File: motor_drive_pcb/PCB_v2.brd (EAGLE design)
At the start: 27 parts, among them IC1 MCP604P, J1 FRDM-K64F

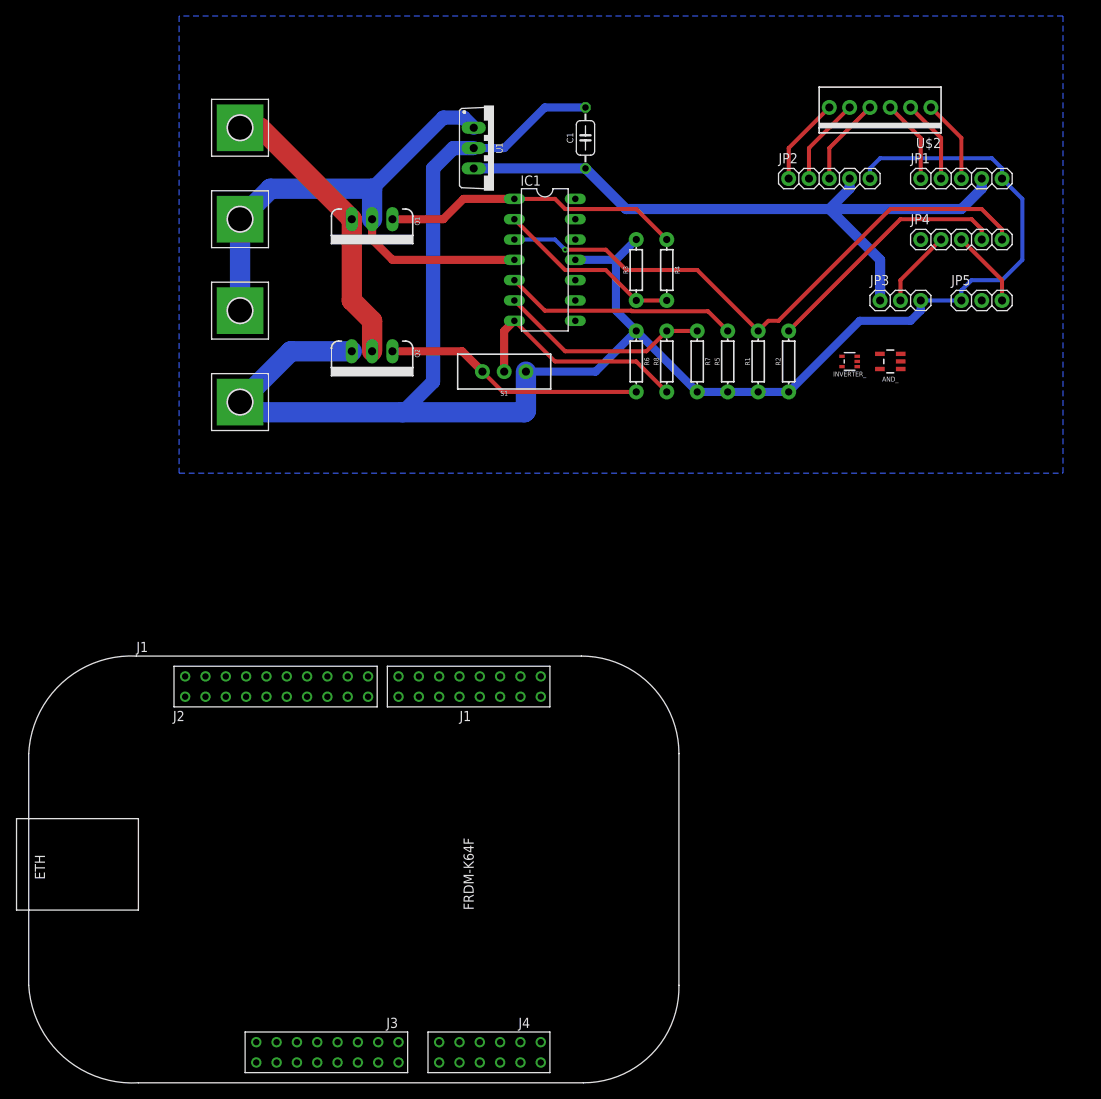
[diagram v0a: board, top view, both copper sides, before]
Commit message: updated pcb and encoder schematics and boards
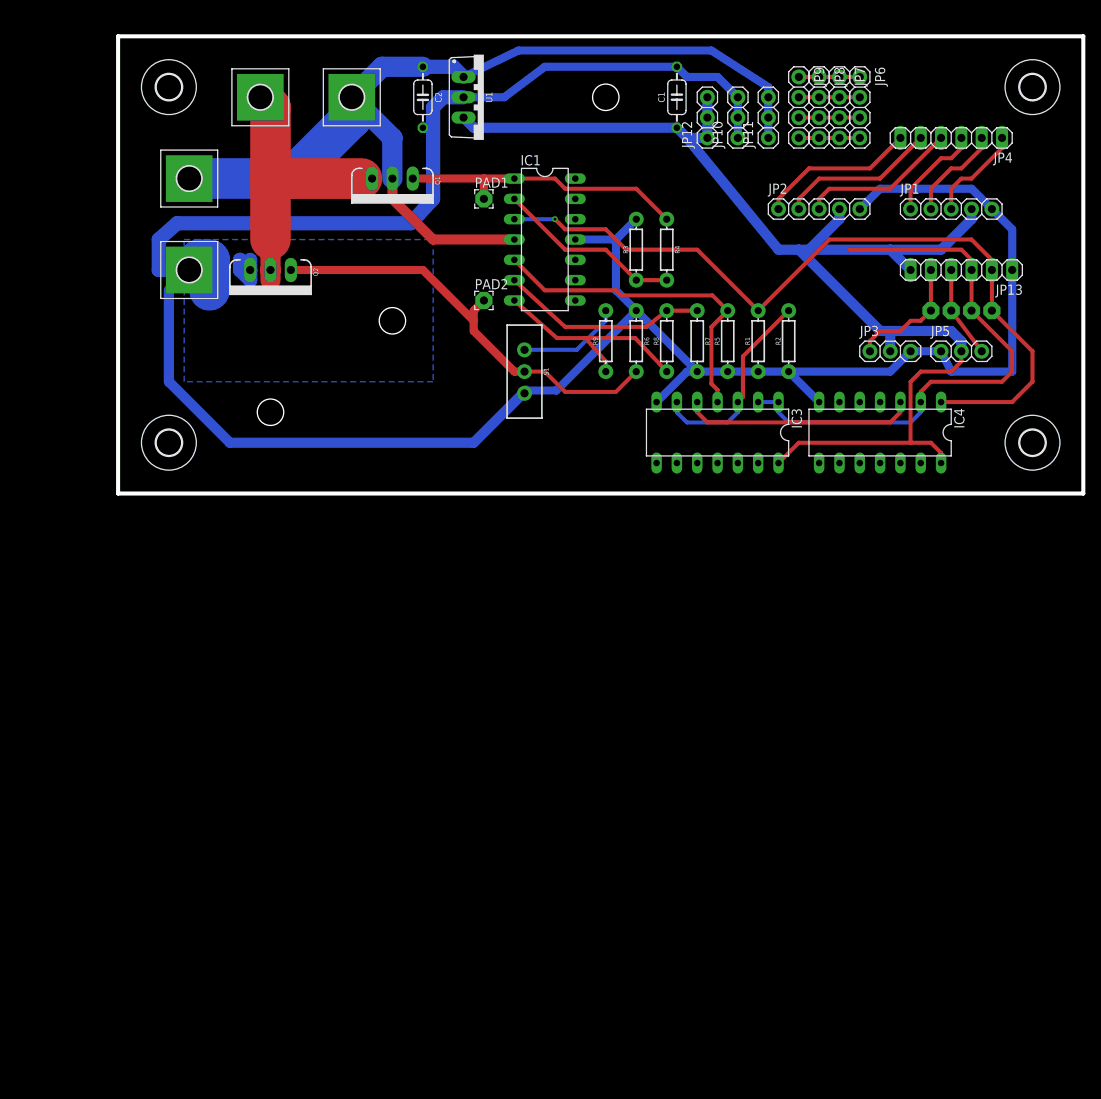
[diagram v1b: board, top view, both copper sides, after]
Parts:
- removed AND_: (no value), SparkFun-IC-Logic:SOT23-5
- removed INVERTER_: (no value), SparkFun-IC-Logic:SOT353
- removed J1: FRDM-K64F, ee192:FRDM-K64F
- removed U$2: M06, ee192:1X06-MTA
- added C2: (no value), bt_rcl:C075
- added H1, H2, H3, H4: MOUNT-HOLE3.2, holes:3,2
- added IC3: 4081N, 40xx:DIL14
- added IC4: 4030N, 40xx:DIL14
- added JP10, JP11, JP12: (no value), ee192:1X03
- added JP13: (no value), pinhead:1X06
- added JP6, JP7, JP8, JP9: (no value), ee192:1X04
- added PAD1, PAD2, PAD3, PAD5, PAD6, PAD7: (no value), wirepad:2,15/1,0
- added R9: 100, SparkFun-Resistors:AXIAL-0.3
- JP4: device ee192:1X05 -> pinhead:1X06
- moved BATT+1 20.7 mm to (-17.8, 45.7)
- moved BATT+ 17.7 mm to (-38.1, 35.6)
- moved BATT- 17.7 mm to (-38.1, 24.1)
- moved Q2 16.3 mm to (-27.9, 24.1)
- moved JP4 12.8 mm to (57.1, 40.6), turned to 180 degrees
- moved C1 12.5 mm to (22.9, 45.7)
- moved JP5 6.84 mm to (58.4, 14.0)
- moved U1 6.48 mm to (-3.81, 45.7)
- moved JP3 6.48 mm to (49.5, 14.0)
- moved Q1 5.68 mm to (-12.7, 35.6)
- moved BATT-1 4.58 mm to (-29.2, 45.7)
- moved JP1 4.02 mm to (57.1, 31.8)
- moved JP2 4.02 mm to (40.6, 31.8)
- moved IC1 2.54 mm to (6.35, 27.9)
- moved R3 2.54 mm to (17.8, 26.7)
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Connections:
- removed net 3.3V: AND_.5, INVERTER_.5, JP4.1
- removed net N$12: JP1.1, U$2.3
- removed net N$13: JP1.2, U$2.2
- removed net N$14: JP1.3, U$2.1
- removed net N$17: AND_.2, JP4.4, R2.P$2
- new net AO1: JP1.1, JP4.3
- new net CL1: JP1.3, JP4.1
- new net N$21: IC3.3, IC3.6, R2.P$2
- new net N$22: JP6.4, JP7.4, JP8.4, JP9.4
- new net N$23: JP6.3, JP7.3, JP8.3, JP9.3
- new net N$24: JP6.2, JP7.2, JP8.2, JP9.2
- new net N$25: JP6.1, JP7.1, JP8.1, JP9.1
- new net N$26: IC3.1, IC3.2, IC4.2, JP13.3, PAD5.1
- new net SI1: JP1.2, JP4.2
- net GND: now also C2.2, IC3.7, IC4.7, JP10.1, JP10.2, JP10.3, JP13.1, S1.1; no longer AND_.3, INVERTER_.3, J1.J2-3, S1.3
- net N$10: now also JP4.5; no longer U$2.5
- net N$11: now also JP4.4; no longer U$2.4
- net N$15: now also JP13.4, PAD7.1; no longer JP4.3
- net N$16: now also IC4.1, JP13.2, PAD6.1; no longer INVERTER_.2, JP4.5
- net N$18: now also IC3.14, IC4.14, JP12.1, JP12.2, JP12.3, JP13.6, JP3.2, JP5.2; no longer JP3.1
- net N$19: now also JP13.5, JP3.1, PAD3.1; no longer JP3.2, JP4.2
- net N$2: now also PAD1.1
- net N$20: now also IC1.5, IC3.4, R5.P$2; no longer JP5.2
- net N$4: now also R9.P$2, S1.3; no longer AND_.4, IC1.5, R5.P$2
- net N$5: now also PAD2.1, S1.2; no longer S1.1
- net N$7: now also R9.P$1; no longer S1.2
- net N$8: now also IC3.5, IC4.3; no longer AND_.1, INVERTER_.4
- net N$9: now also JP4.6; no longer U$2.6
- net V_BATT: now also C2.1, JP11.1, JP11.2, JP11.3
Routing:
- net GND: track 237.7 -> 327.5 mm
- net N$18: track 86.8 -> 160.2 mm
- net N$26: track 0.00 -> 69.5 mm
- net V_BATT: track 72.0 -> 122.1 mm
- net N$20: track 0.00 -> 41.9 mm
- net N$17: track 31.7 -> 0.00 mm
- net N$8: track 0.00 -> 29.0 mm
- net N$21: track 0.00 -> 25.3 mm
- net N$16: track 74.3 -> 99.0 mm
- net N$5: track 32.6 -> 54.4 mm
- net N$4: track 29.3 -> 12.9 mm
- net SI1: track 0.00 -> 12.3 mm
- net CL1: track 0.00 -> 12.3 mm
- net AO1: track 0.00 -> 12.3 mm
- net N$14: track 10.5 -> 0.00 mm
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- added copper zone on layer 16, net GND
- removed copper zone on layer 16, net N$21
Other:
- board outline added: 120.7 x 57.2 mm
